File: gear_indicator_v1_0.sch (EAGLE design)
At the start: 24 parts, among them IC1 NE555, IC2 74ALS08N, IC3 74ALS04N, IC4 7805TV, J1 POWER_JACKPTH, J2 TERMBLOCKX8, T1 2N3904, T2 2N3904, T3 2N3904

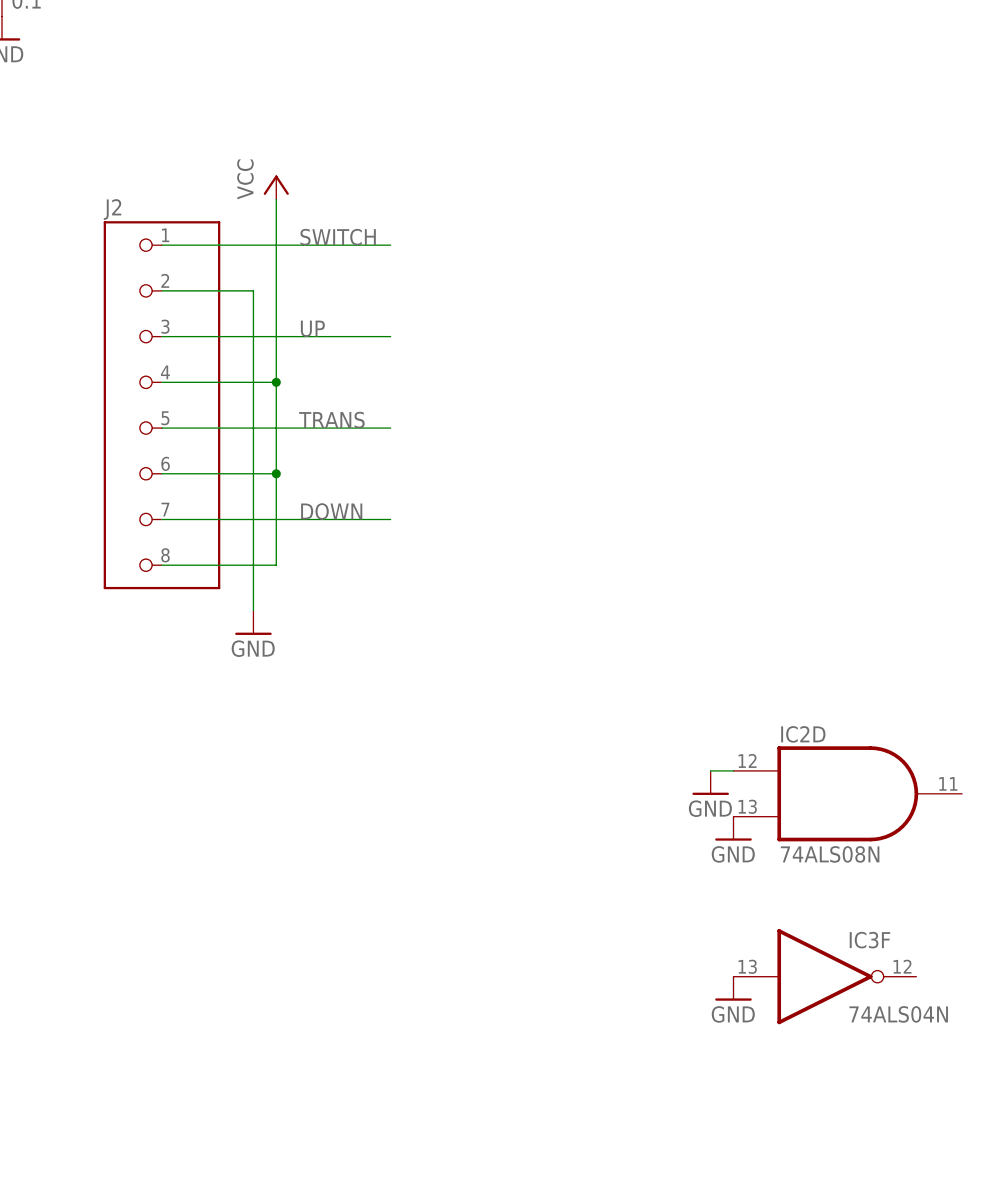
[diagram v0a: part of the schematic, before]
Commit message: Fixed tie to ground for unused logic gates Added low pass filter on switch input
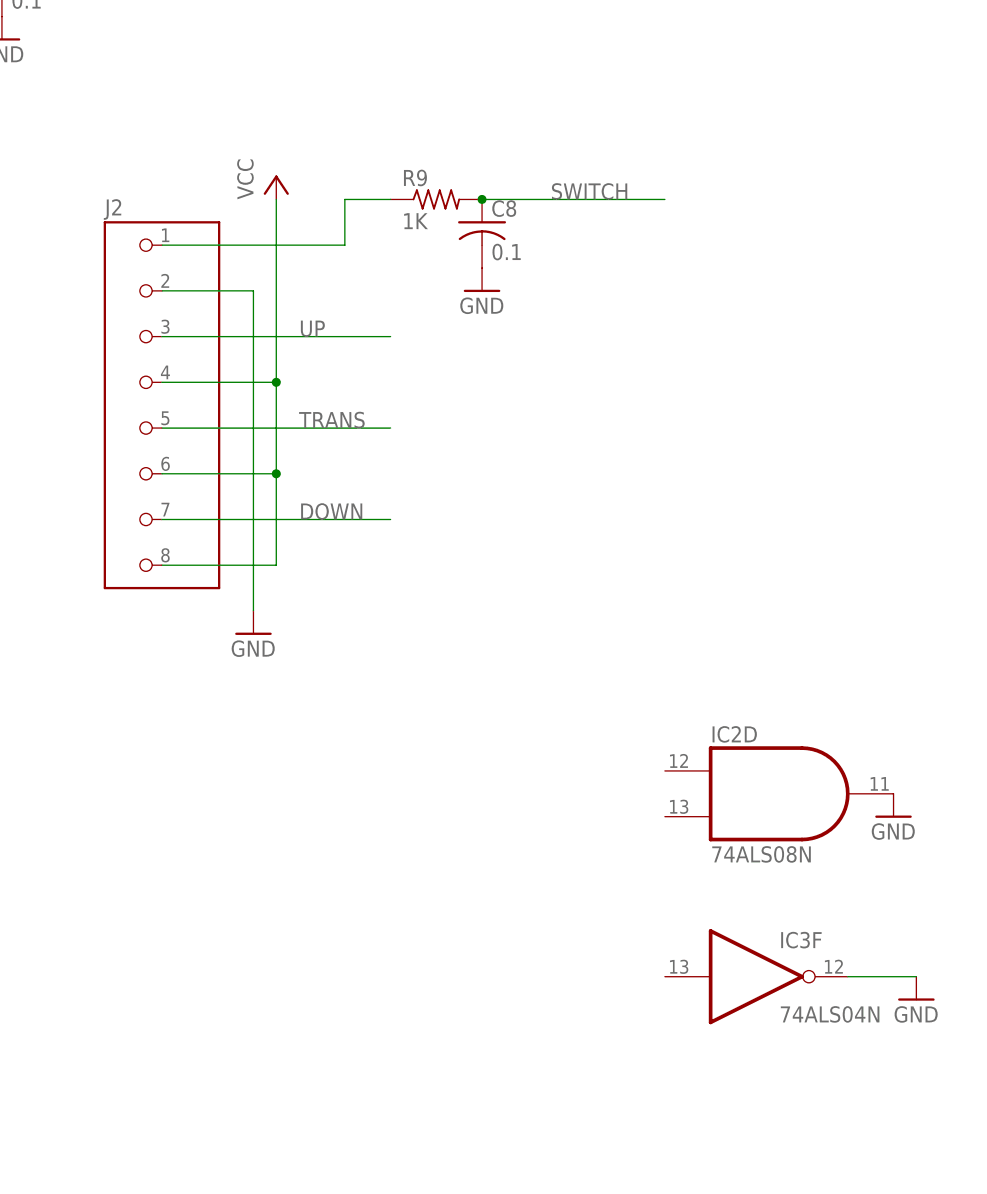
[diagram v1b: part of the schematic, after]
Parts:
- added C8: 0.1, resistor:C-US025-025X050
- added R9: 1K, resistor:R-US_0207/10
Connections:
- new net N$17: J2.1, R9.1
- net GND: now also C8.2, IC2D.O, IC3F.O; no longer IC2D.I0, IC2D.I1, IC3F.I
- net SWITCH: now also C8.1, R9.2; no longer J2.1
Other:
- moved on the sheet: IC2D, IC3F
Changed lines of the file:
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@@
 <part name="C5" library="resistor" deviceset="C-US" device="025-025X050" value="0.1"/>
 <part name="VSS8" library="supply1" deviceset="GND" device=""/>
-<part name="VSS9" library="supply1" deviceset="GND" device=""/>
-<part name="VSS10" library="supply1" deviceset="GND" device=""/>
-<part name="VSS11" library="supply1" deviceset="GND" device=""/>
 <part name="J1" library="SparkFun" deviceset="POWER_JACK" device="PTH" value=""/>
 <part name="VSS13" library="supply1" deviceset="GND" device=""/>
@@
 <part name="C6" library="resistor" deviceset="C-US" device="025-025X050" value="0.1"/>
 <part name="C7" library="resistor" deviceset="C-US" device="025-025X050" value="0.1"/>
+<part name="VSS10" library="supply1" deviceset="GND" device=""/>
+<part name="VSS11" library="supply1" deviceset="GND" device=""/>
+<part name="R9" library="resistor" deviceset="R-US_" device="0207/10" value="1K"/>
+<part name="C8" library="resistor" deviceset="C-US" device="025-025X050" value="0.1"/>
+<part name="VSS9" library="supply1" deviceset="GND" device=""/>
 </parts>
 <sheets>
@@
 <instance part="IC2" gate="B" x="63.5" y="20.32"/>
 <instance part="IC2" gate="C" x="152.4" y="172.72"/>
-<instance part="IC2" gate="D" x="233.68" y="63.5"/>
+<instance part="IC2" gate="D" x="226.06" y="63.5"/>
 <instance part="IC2" gate="P" x="83.82" y="127"/>
 <instance part="IC3" gate="A" x="30.48" y="45.72"/>
@@
 <instance part="IC3" gate="D" x="124.46" y="165.1"/>
 <instance part="IC3" gate="E" x="175.26" y="172.72"/>
-<instance part="IC3" gate="F" x="231.14" y="43.18"/>
+<instance part="IC3" gate="F" x="223.52" y="43.18"/>
 <instance part="IC3" gate="P" x="106.68" y="127"/>
 <instance part="R1" gate="G$1" x="12.7" y="101.6"/>
@@
 <instance part="C5" gate="G$1" x="139.7" y="154.94"/>
 <instance part="VSS8" gate="1" x="139.7" y="147.32"/>
-<instance part="VSS9" gate="1" x="220.98" y="40.64"/>
-<instance part="VSS10" gate="1" x="220.98" y="58.42"/>
-<instance part="VSS11" gate="1" x="218.44" y="63.5"/>
 <instance part="J1" gate="G$1" x="17.78" y="162.56"/>
 <instance part="VSS13" gate="1" x="20.32" y="162.56"/>
@@
 <instance part="C6" gate="G$1" x="91.44" y="127"/>
 <instance part="C7" gate="G$1" x="114.3" y="127"/>
+<instance part="VSS10" gate="1" x="238.76" y="60.96"/>
+<instance part="VSS11" gate="1" x="241.3" y="40.64"/>
+<instance part="R9" gate="G$1" x="187.96" y="129.54"/>
+<instance part="C8" gate="G$1" x="193.04" y="127"/>
+<instance part="VSS9" gate="1" x="193.04" y="119.38"/>
 </instances>
 <busses>
@@
 </segment>
 <segment>
-<pinref part="IC3" gate="F" pin="I"/>
-<pinref part="VSS9" gate="1" pin="GND"/>
-</segment>
-<segment>
-<pinref part="IC2" gate="D" pin="I1"/>
-<pinref part="VSS10" gate="1" pin="GND"/>
-</segment>
-<segment>
-<wire x1="218.44" y1="66.04" x2="220.98" y2="66.04" width="0.1524" layer="91"/>
-<pinref part="IC2" gate="D" pin="I0"/>
-<pinref part="VSS11" gate="1" pin="GND"/>
-</segment>
-<segment>
 <wire x1="20.32" y1="167.64" x2="20.32" y2="165.1" width="0.1524" layer="91"/>
 <junction x="20.32" y="165.1"/>
@@
 <pinref part="J2" gate="G$1" pin="2"/>
 <pinref part="VSS12" gate="1" pin="GND"/>
+</segment>
+<segment>
+<pinref part="IC2" gate="D" pin="O"/>
+<pinref part="VSS10" gate="1" pin="GND"/>
+</segment>
+<segment>
+<pinref part="IC3" gate="F" pin="O"/>
+<pinref part="VSS11" gate="1" pin="GND"/>
+<wire x1="233.68" y1="43.18" x2="241.3" y2="43.18" width="0.1524" layer="91"/>
+</segment>
+<segment>
+<pinref part="VSS9" gate="1" pin="GND"/>
+<pinref part="C8" gate="G$1" pin="2"/>
 </segment>
 </net>
@@
 </segment>
 <segment>
-<wire x1="182.88" y1="124.46" x2="157.48" y2="124.46" width="0.1524" layer="91"/>
-<label x="172.72" y="124.46" size="1.778" layer="95"/>
-<pinref part="J2" gate="G$1" pin="1"/>
+<pinref part="R9" gate="G$1" pin="2"/>
+<pinref part="C8" gate="G$1" pin="1"/>
+<wire x1="193.04" y1="129.54" x2="213.36" y2="129.54" width="0.1524" layer="91"/>
+<junction x="193.04" y="129.54"/>
+<label x="200.66" y="129.54" size="1.778" layer="95"/>
 </segment>
 </net>
@@
 </segment>
 </net>
+<net name="N$17" class="0">
+<segment>
+<pinref part="J2" gate="G$1" pin="1"/>
+<wire x1="157.48" y1="124.46" x2="177.8" y2="124.46" width="0.1524" layer="91"/>
+<wire x1="177.8" y1="124.46" x2="177.8" y2="129.54" width="0.1524" layer="91"/>
+<pinref part="R9" gate="G$1" pin="1"/>
+<wire x1="177.8" y1="129.54" x2="182.88" y2="129.54" width="0.1524" layer="91"/>
+</segment>
+</net>

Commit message: layout tweaks
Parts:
- added LED1: Power, dp_devices:LED3MM
- added R10: 220, resistor:R-US_0207/7
- C3: device rcl:CPOL-USE2.5-6 -> rcl:CPOL-USE3.5-10
- R1, R3, R4, R5, R6, R7, R8, R9: device resistor:R-US_0207/10 -> resistor:R-US_0207/7
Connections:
- new net N$16: LED1.C, R10.2
- net GND: now also R10.1
- net VCC: now also LED1.A
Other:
- moved on the sheet: C6, C7, IC2P, IC3P
